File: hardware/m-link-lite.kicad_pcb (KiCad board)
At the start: 2 copper layers, 24 x 30 mm, 22 parts, among them J1 BEC IN, J2 PROGRAM, J3 SIG, U1 AP1117-50, U2 MCP1702-3v3, U3 74LS365, U4 ESP-12F

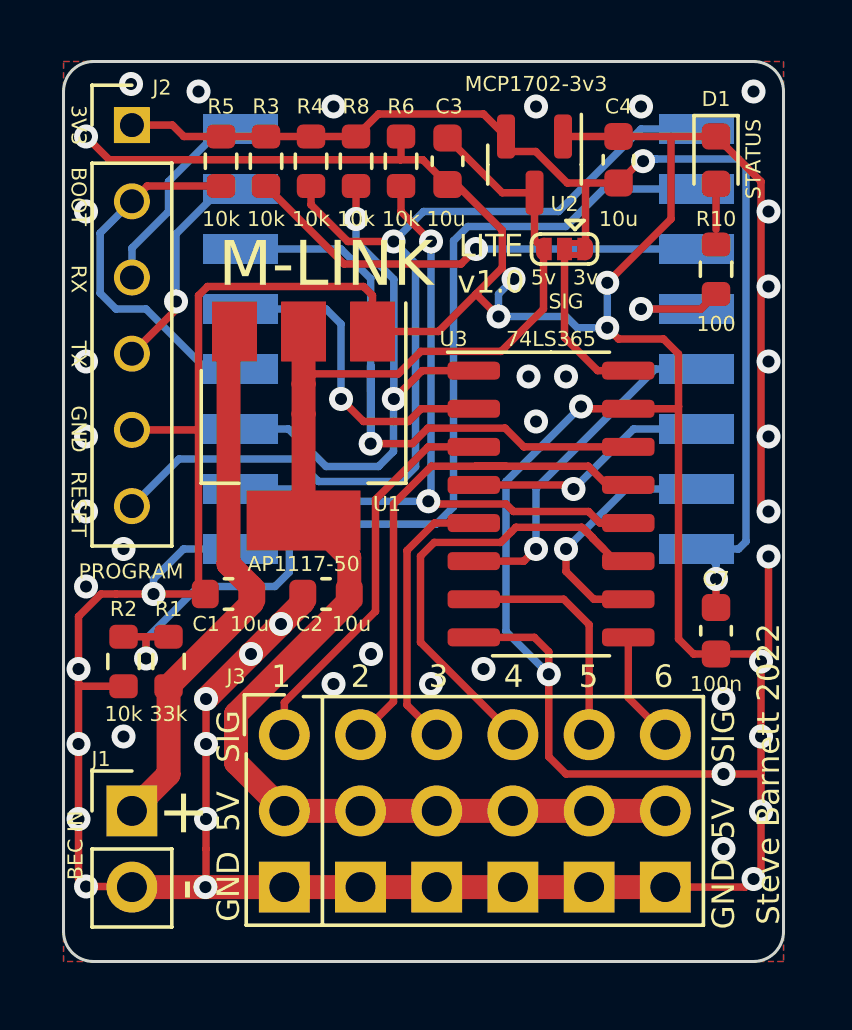
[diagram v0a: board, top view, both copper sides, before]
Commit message: Power supply rework.
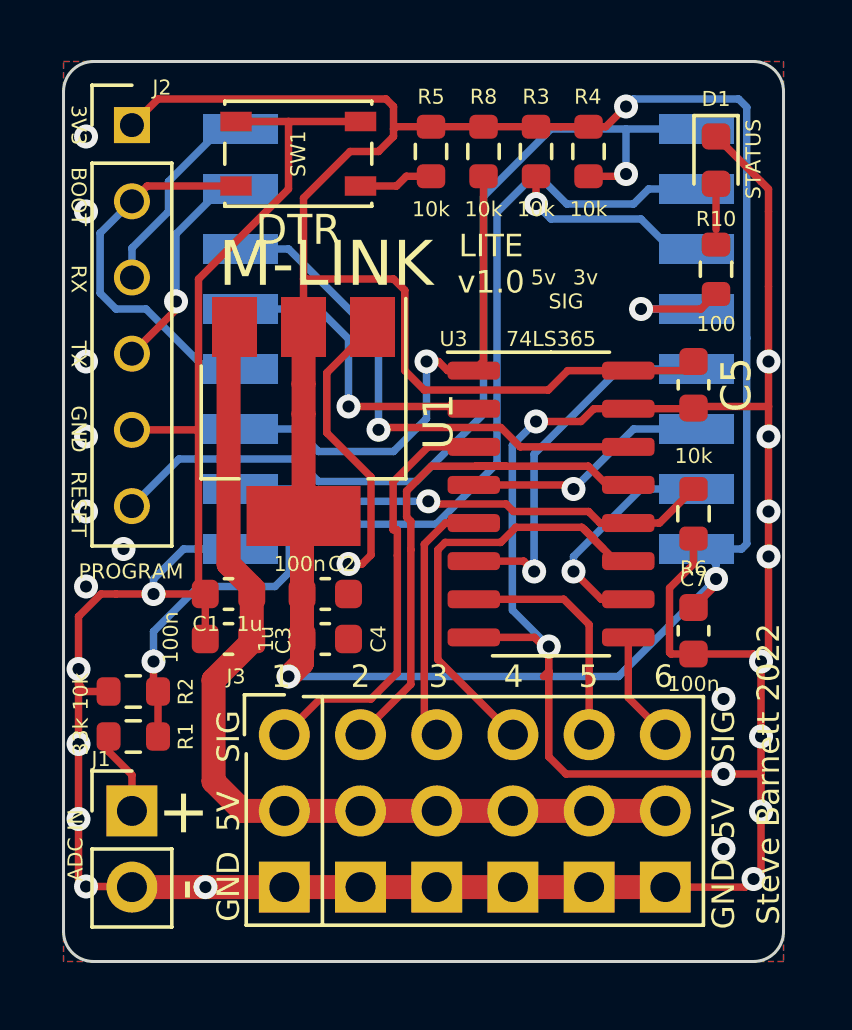
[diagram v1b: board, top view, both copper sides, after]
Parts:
- removed JP1: VSIG, Jumper:SolderJumper-3_P1.3mm_Bridged2Bar12_RoundedPad1.0x1.5mm
- removed U2: MCP1702-3v3, Package_TO_SOT_SMD:SOT-23
- added C5: 100n, Capacitor_SMD:C_0603_1608Metric, F.Cu at (100.0, 79.8)
- added SW1: DTR, new_moop_items:SW_SPST_PTS810, F.Cu at (86.8, 72.1)
- C1, C4: value 10u -> 1u
- C2, C3: value 10u -> 100n
- J1: value BEC IN -> ADC IN
- U1: value AP1117-50 -> AP1117-33
- moved C4 18.7 mm to (87.7, 88.2), turned to 0 degrees
- moved C3 17.5 mm to (84.5, 88.2), turned to 180 degrees
- moved R6 15.3 mm to (100.0, 84.1), turned to -90 degrees
- moved R4 9.26 mm to (96.5, 72.0)
- moved R3 9.01 mm to (94.8, 72.0)
- moved R5 7.01 mm to (91.2, 72.0)
- moved R8 4.26 mm to (93.0, 72.0)
- moved R1 2.76 mm to (81.3, 91.5), turned to 0 degrees
- moved R2 1.05 mm to (81.3, 90.0), turned to 180 degrees
- moved C7 0.75 mm to (100.0, 88.0)
- moved U1 0.15 mm to (87.0, 81.0)
- turned C2 to 0 degrees
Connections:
- C1 pad 1: /VCC -> +5V
- C2 pad 1: +5V -> +3V3
- C4 pad 1: /3V3 -> +3V3
- C7 pad 1: /3V3 -> +3V3
- J1 pad 1: /VCC -> /SENSE
- J2 pad 1: /3V3 -> +3V3
- R1 pad 1: /VCC -> /SENSE
- R3 pad 1: /3V3 -> +3V3
- R4 pad 1: /3V3 -> +3V3
- R5 pad 1: /3V3 -> +3V3
- R8 pad 1: /3V3 -> +3V3
- U1 pad 2: +5V -> +3V3
- U1 pad 3: /VCC -> +5V
- U3 pad 16: Net-(U3-Pad16) -> +3V3
- U4 pad 8: /3V3 -> +3V3
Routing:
- net +3V3: track 0.00 -> 93.8 mm, vias 0 -> 3
- net /3V3: track 41.3 -> 0.00 mm, vias 2 -> 0
- net GND: track 180.4 -> 139.8 mm, vias 51 -> 27
- net /VCC: track 18.0 -> 0.00 mm
- net +5V: track 48.4 -> 31.4 mm
- net /EN: track 15.6 -> 6.90 mm
- net /CH4_LV: track 24.4 -> 16.3 mm, vias 2 -> 1
- net /CH2_LV: track 25.1 -> 17.8 mm
- net Net-(U3-Pad16): track 5.53 -> 0.00 mm
- net /DTR: track 12.4 -> 15.4 mm
- net /SENSE: track 0.00 -> 2.80 mm
- net /RESET: track 34.0 -> 31.9 mm
- net /CH5_LV: track 11.3 -> 12.7 mm
- net /CH1: track 13.1 -> 14.3 mm
- net /OE: track 18.0 -> 17.2 mm, vias 2 -> 1
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
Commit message: Rework v1.2 layout.
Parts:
- SW1: value DTR -> RESTORE SETTINGS
- moved C5 7.84 mm to (99.2, 72.0)
- moved R6 3.93 mm to (100.5, 80.2), turned to 90 degrees
- moved U3 2.30 mm to (95.9, 81.6)
- moved U1 2.25 mm to (87.0, 78.8)
- moved C2 2.14 mm to (88.5, 84.8)
- moved C3 2.14 mm to (85.3, 86.2)
- moved C4 2.14 mm to (88.5, 86.2)
- moved C1 2.14 mm to (85.2, 84.8)
- moved R10 1.01 mm to (101.5, 75.2)
- moved D1 0.79 mm to (101.5, 72.0)
- moved C7 0.50 mm to (100.5, 88.0)
- moved R2 0.50 mm to (81.3, 89.5)
- moved R1 0.25 mm to (81.3, 91.2)
- moved SW1 0.10 mm to (86.9, 72.1), turned to 180 degrees
- turned R5 to 90 degrees
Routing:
- net GND: track 139.8 -> 101.6 mm, vias 27 -> 45
- net +3V3: track 93.8 -> 61.3 mm, vias 3 -> 2
- net /DTR: track 15.4 -> 21.1 mm
- net /CH3: track 8.46 -> 12.0 mm
- net +5V: track 31.4 -> 34.5 mm
- net /CH5: track 7.87 -> 10.7 mm
- net /CH5_LV: track 12.7 -> 9.83 mm
- net /RESET: track 31.9 -> 29.2 mm
- net /EN: track 6.90 -> 9.60 mm
- net /CH1: track 14.3 -> 16.6 mm
- net /CH6: track 3.76 -> 5.67 mm
- net /ADC: track 34.1 -> 32.4 mm
- net /CH6_LV: track 7.74 -> 6.21 mm
- net /CH3_LV: track 8.31 -> 6.89 mm
- net /LED1: track 4.56 -> 3.28 mm
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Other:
- board text added: "LITE v1.1"
- board text removed: "+"
- board text removed: "-"
- board text removed: "3v"
- board text removed: "5v"
- board text removed: "LITE v1.0"

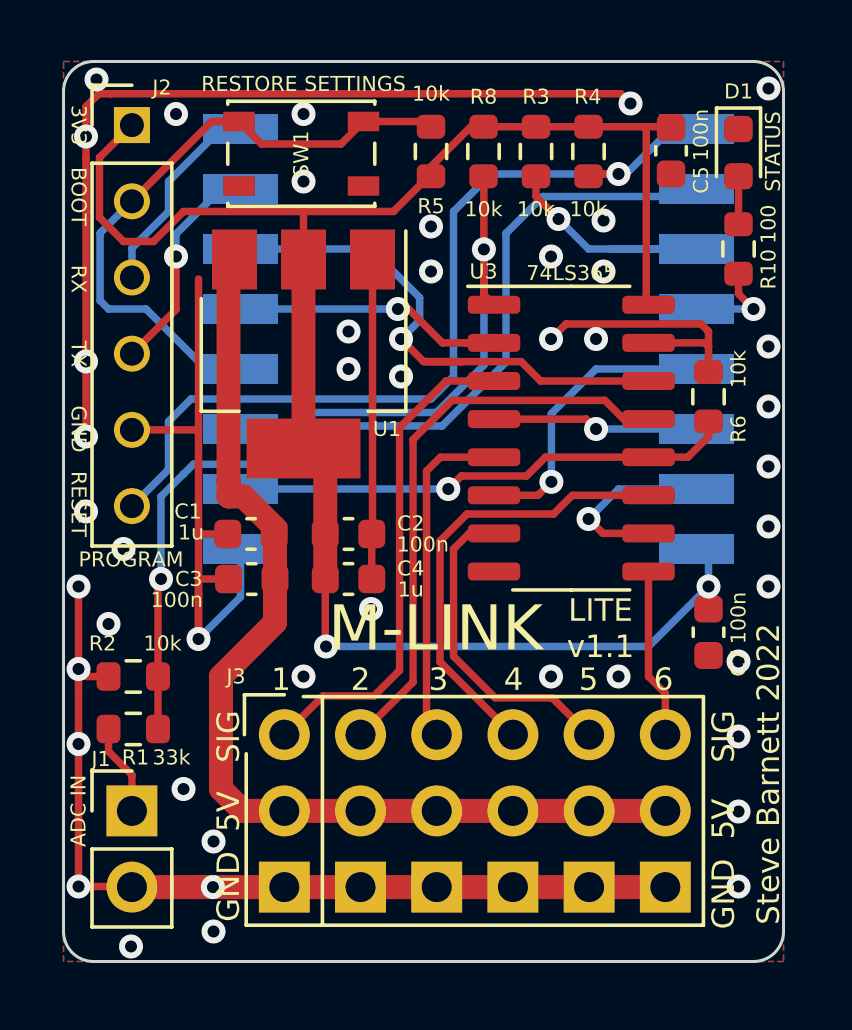
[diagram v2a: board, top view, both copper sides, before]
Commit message: Rotate regulator 180.
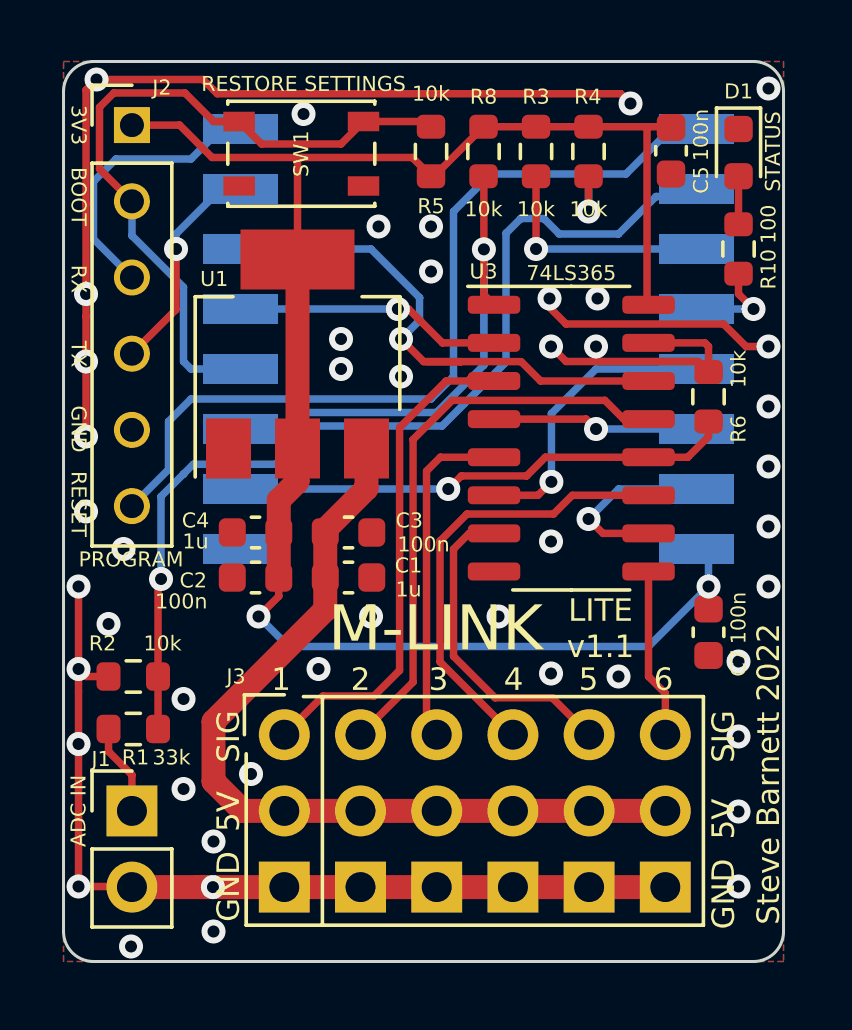
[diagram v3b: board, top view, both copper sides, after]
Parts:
- moved C3 3.58 mm to (88.5, 84.7), turned to 0 degrees
- moved C1 3.56 mm to (88.5, 86.2), turned to 0 degrees
- moved C4 3.47 mm to (85.4, 84.7), turned to 180 degrees
- moved C2 3.42 mm to (85.4, 86.2), turned to 180 degrees
- moved U1 0.20 mm to (86.8, 78.8), turned to 90 degrees
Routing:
- net GND: track 101.6 -> 77.7 mm, vias 45 -> 46
- net +5V: track 34.5 -> 28.7 mm
- net /DTR: track 21.1 -> 24.0 mm
- net /RX: track 6.83 -> 9.36 mm
- net /EN: track 9.60 -> 7.77 mm
- net +3V3: track 61.3 -> 59.6 mm
- net /RESET: track 29.2 -> 30.6 mm
- net /CH1_LV: track 9.89 -> 8.92 mm

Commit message: Tidy up.
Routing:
- net /RESET: track 30.6 -> 28.7 mm
- net /ADC: track 32.8 -> 32.1 mm
- net GND: vias 46 -> 48

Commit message: Layout tweaks.
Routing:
- net /CH5: track 10.7 -> 8.98 mm
- net /ADC: track 32.1 -> 33.3 mm
- net /CH1: track 16.6 -> 15.6 mm
- net /OE: track 17.3 -> 17.8 mm
- net GND: vias 48 -> 49

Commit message: Plot v1.1.
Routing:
- net GND: track 77.7 -> 79.7 mm, vias 49 -> 48
- net /CH3: track 12.0 -> 11.4 mm
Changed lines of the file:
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@@
     (pad "4" smd rect (at -7.6 -2.5 180) (size 2.5 1) (layers "B.Cu" "B.Paste" "B.Mask")
       (net 18 "/LED1") (pinfunction "GPIO16") (pintype "bidirectional"))
-    (pad "5" smd rect (at -7.6 -4.5 180) (size 2.5 1) (layers "B.Cu" "B.Paste" "B.Mask")
+    (pad "5" smd rect (at -7.6 -4.5 180) (size 4 1) (layers "B.Cu" "B.Paste" "B.Mask")
       (net 23 "/CH5_LV") (pinfunction "GPIO14") (pintype "bidirectional"))
     (pad "6" smd rect (at -7.6 -6.5 180) (size 2.5 1) (layers "B.Cu" "B.Paste" "B.Mask")
       (net 21 "/CH3_LV") (pinfunction "GPIO12") (pintype "bidirectional"))
-    (pad "7" smd rect (at -7.6 -8.5 180) (size 2.5 1) (layers "B.Cu" "B.Paste" "B.Mask")
+    (pad "7" smd rect (at -7.6 -8.5 180) (size 4 1) (layers "B.Cu" "B.Paste" "B.Mask")
       (net 16 "/CH6_LV") (pinfunction "GPIO13") (pintype "bidirectional"))
     (pad "8" smd rect (at -7.6 -10.5 180) (size 2.5 1) (layers "B.Cu" "B.Paste" "B.Mask")
@@
   (segment (start 80.5 89.5) (end 79.75 89.5) (width 0.25) (layer "F.Cu") (net 1))
   (segment (start 79.75 79) (end 79.75 77.5) (width 0.25) (layer "F.Cu") (net 1))
+  (segment (start 102.5 78.5) (end 102.5 80.5) (width 0.25) (layer "F.Cu") (net 1))
   (segment (start 101.75 78.5) (end 102.5 78.5) (width 0.25) (layer "F.Cu") (net 1))
   (segment (start 93.98 96.52) (end 96.52 96.52) (width 0.8) (layer "F.Cu") (net 1))
@@
   (via (at 87 70.75) (size 0.8) (drill 0.4) (layers "F.Cu" "B.Cu") (free) (net 1))
   (via (at 95.2 76.9) (size 0.8) (drill 0.4) (layers "F.Cu" "B.Cu") (free) (net 1))
-  (via (at 102.5 78.5) (size 0.8) (drill 0.4) (layers "F.Cu" "B.Cu") (free) (net 1))
-  (via (at 102.5 82.5) (size 0.8) (drill 0.4) (layers "F.Cu" "B.Cu") (free) (net 1))
+  (via (at 102.5 82) (size 0.8) (drill 0.4) (layers "F.Cu" "B.Cu") (free) (net 1))
   (via (at 79.5 91.75) (size 0.8) (drill 0.4) (layers "F.Cu" "B.Cu") (net 1))
   (via (at 102.5 80.5) (size 0.8) (drill 0.4) (layers "F.Cu" "B.Cu") (free) (net 1))
@@
   (segment (start 91.56 82.19) (end 91.10096 82.64904) (width 0.25) (layer "F.Cu") (net 11))
   (segment (start 91.45192 87.04808) (end 91.44 87.06) (width 0.25) (layer "F.Cu") (net 11))
-  (segment (start 91.02596 91.02596) (end 91.44 91.44) (width 0.25) (layer "F.Cu") (net 11))
   (segment (start 91.10096 84.14904) (end 91.45192 84.5) (width 0.25) (layer "F.Cu") (net 11))
   (segment (start 96.52 91.44) (end 96.52 86.27) (width 0.25) (layer "F.Cu") (net 12))
